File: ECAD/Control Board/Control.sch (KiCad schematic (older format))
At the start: 1 part

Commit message: control
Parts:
- added J?: FAN, symbol Connector:Conn_01x02_Female
- added Q? (x2): 2N7002, Package_TO_SOT_SMD:SOT-23, symbol Transistor_FET:2N7002
- added Q?: IRF7425, Package_SO:SOIC-8_3.9x4.9mm_P1.27mm, symbol Transistor_FET:IRF7404
- added R? (x2): 10K, symbol Device:R
- added R?: 100R, symbol Device:R
- added SW?: EN, symbol Switch:SW_SPST
- added SW?: Rotary_Encoder_Switch, symbol Device:Rotary_Encoder_Switch
- added U?: STM32BluePill, symbol symbols:STM32BluePill
- added U?: RC1602A, Display:RC1602A, symbol Display_Character:RC1602A
- added U?: 74HC595, symbol 74xx:74HC595
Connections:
- net +5V: now also Q?.5 (D), Q?.6 (D), Q?.7 (D), Q?.8 (D), R?.1, U?.18 (5V)
- net EN: now also Q?.3 (D), SW?.2 (B)
- net GND: now also Q?.2 (S), SW?.1 (A), U?.19 (GND), U?.39 (GND), U?.40 (GND)
- net IOUTBUF: now also U?.27 (PA2)
- net I_IN: now also U?.25 (PA0)
- net M_CS0: now also U?.13 (PB5)
- net M_CS1: now also U?.12 (PB4)
- net M_LDAC0: now also U?.11 (PB3)
- net M_LDAC1: now also U?.10 (PA15)
- net M_MOSI: now also U?.32 (PA7)
- net M_SCK: now also U?.30 (PA5)
- net VIN_BUF: now also U?.26 (PA1)
- net VOUTBUF: now also U?.28 (PA3)
- new net: Q?.1 (G), U?.5 (PA8)
- new net: J?.1 (Pin_1), Q?.1 (S), Q?.2 (S), Q?.3 (S)
- new net: Q?.3 (D), Q?.4 (G), R?.2
- new net: J?.2 (Pin_2), Q?.2 (S), R?.2
- new net: Q?.1 (G), R?.1, R?.2
- new net DISP0: U?.15 (QA), U?.7 (DB0)
- new net DISP1: U?.1 (QB), U?.8 (DB1)
- new net DISP2: U?.2 (QC), U?.9 (DB2)
- new net DISP3: U?.10 (DB3), U?.3 (QD)
- new net DISP4: U?.11 (DB4), U?.4 (QE)
- new net DISP5: U?.12 (DB5), U?.5 (QF)
- new net DISP6: U?.13 (DB6), U?.6 (QG)
- new net DISP7: U?.14 (DB7), U?.7 (QH)
- new net FAN: R?.1, U?.33 (PB0)

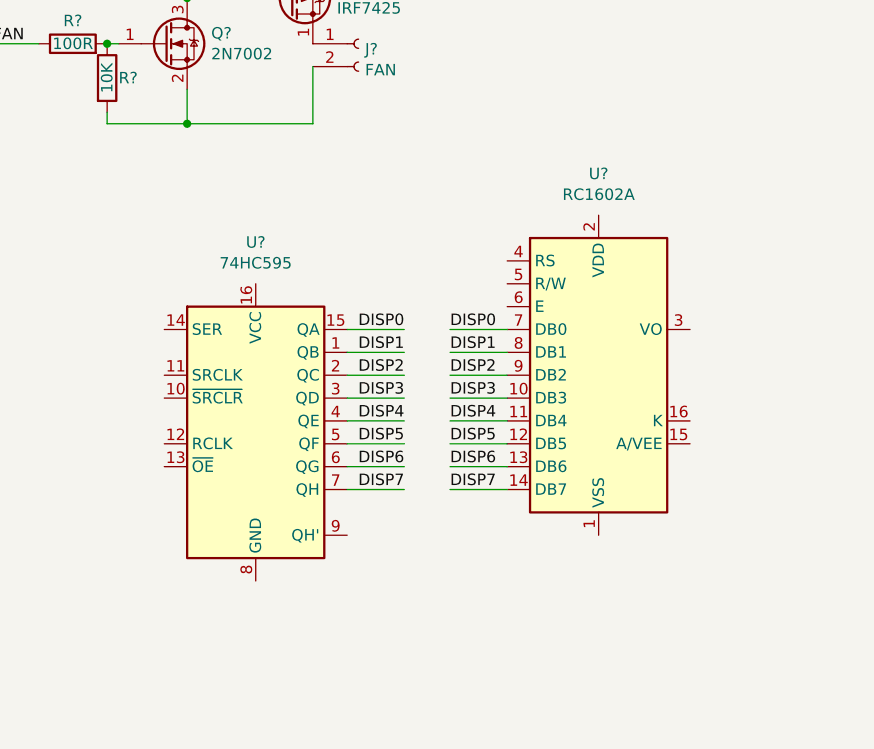
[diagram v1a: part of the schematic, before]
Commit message: connect parallel side of shift register
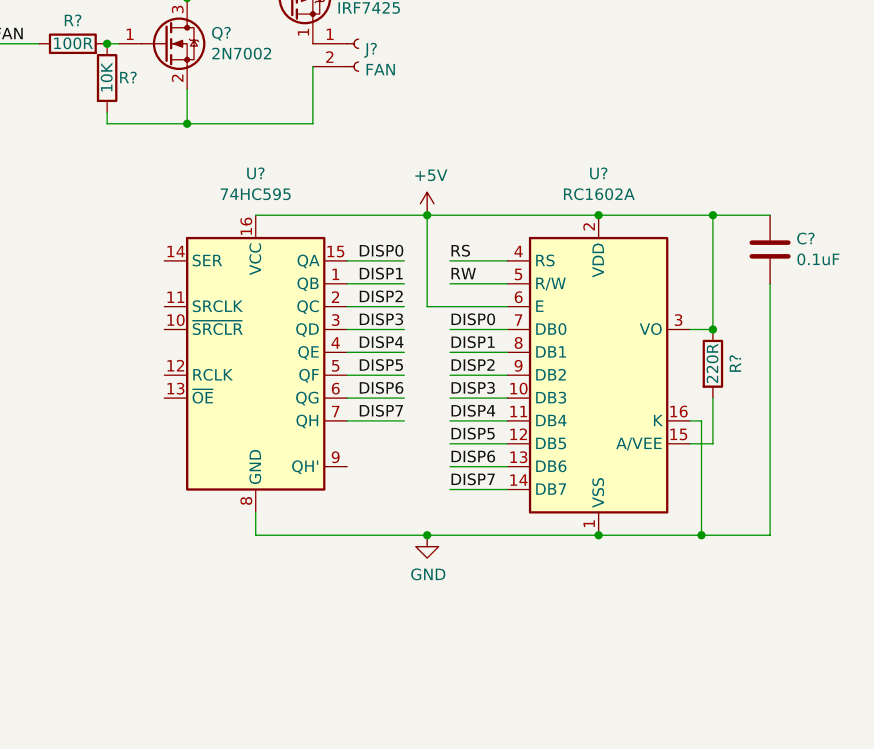
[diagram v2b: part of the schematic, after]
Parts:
- added C?: 0.1uF, symbol Device:C
- added R?: 220R, symbol Device:R
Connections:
- net +5V: now also U?.16 (VCC), U?.2 (VDD), U?.3 (VO), U?.6 (E), C?.1, R?.1
- net GND: now also U?.1 (VSS), U?.16 (K), U?.8 (GND), C?.2
- net at U?.15 (A/VEE): now also R?.2
- net RS: now reaches U?.4 (RS)
- net RW: now reaches U?.5 (R/W)
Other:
- moved on the sheet: U?
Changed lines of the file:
@@
 $EndComp
 Wire Wire Line
-	8500 3200 8250 3200
-Wire Wire Line
-	8500 3300 8250 3300
-Text Label 8500 3200 2    50   ~ 0
+	8500 2900 8250 2900
+Wire Wire Line
+	8500 3000 8250 3000
+Text Label 8500 2900 2    50   ~ 0
 DISP0
-Text Label 8500 3300 2    50   ~ 0
+Text Label 8500 3000 2    50   ~ 0
 DISP1
-Text Label 8500 3400 2    50   ~ 0
+Text Label 8500 3100 2    50   ~ 0
 DISP2
 Wire Wire Line
@@
 L 74xx:74HC595 U?
 U 1 1 62096F8C
-P 7850 3600
-F 0 "U?" H 7850 4381 50  0000 C CNN
-F 1 "74HC595" H 7850 4290 50  0000 C CNN
-F 2 "" H 7850 3600 50  0001 C CNN
-F 3 "http://www.ti.com/lit/ds/symlink/sn74hc595.pdf" H 7850 3600 50  0001 C CNN
-	1    7850 3600
-	1    0    0    -1
-$EndComp
-Text Label 8500 3900 2    50   ~ 0
+P 7850 3300
+F 0 "U?" H 7850 4081 50  0000 C CNN
+F 1 "74HC595" H 7850 3990 50  0000 C CNN
+F 2 "" H 7850 3300 50  0001 C CNN
+F 3 "http://www.ti.com/lit/ds/symlink/sn74hc595.pdf" H 7850 3300 50  0001 C CNN
+	1    7850 3300
+	1    0    0    -1
+$EndComp
+Text Label 8500 3600 2    50   ~ 0
 DISP7
-Text Label 8500 3800 2    50   ~ 0
+Text Label 8500 3500 2    50   ~ 0
 DISP6
-Text Label 8500 3700 2    50   ~ 0
+Text Label 8500 3400 2    50   ~ 0
 DISP5
-Text Label 8500 3600 2    50   ~ 0
+Text Label 8500 3300 2    50   ~ 0
 DISP4
 Wire Wire Line
-	8500 3900 8250 3900
-Wire Wire Line
-	8500 3800 8250 3800
-Wire Wire Line
-	8500 3700 8250 3700
-Wire Wire Line
 	8500 3600 8250 3600
 Wire Wire Line
-	8250 3400 8500 3400
-Text Label 8500 3500 2    50   ~ 0
+	8500 3500 8250 3500
+Wire Wire Line
+	8500 3400 8250 3400
+Wire Wire Line
+	8500 3300 8250 3300
+Wire Wire Line
+	8250 3100 8500 3100
+Text Label 8500 3200 2    50   ~ 0
 DISP3
 Wire Wire Line
-	8500 3500 8250 3500
+	8500 3200 8250 3200
 $Comp
 L Device:Rotary_Encoder_Switch SW?
@@
 	1    0    0    -1
 $EndComp
+Wire Wire Line
+	8700 3000 8950 3000
+Wire Wire Line
+	8950 2900 8700 2900
+Text Label 8700 3000 0    50   ~ 0
+RW
+Text Label 8700 2900 0    50   ~ 0
+RS
+Wire Wire Line
+	8600 3100 8600 2700
+Wire Wire Line
+	8600 2700 7850 2700
+Wire Wire Line
+	8600 3100 8950 3100
+Wire Wire Line
+	8600 2700 9350 2700
+Connection ~ 8600 2700
+Wire Wire Line
+	7850 4000 7850 4100
+Wire Wire Line
+	7850 4100 8600 4100
+Wire Wire Line
+	9750 3200 9850 3200
+Wire Wire Line
+	9850 3200 9850 2700
+Wire Wire Line
+	9850 2700 9350 2700
+Connection ~ 9350 2700
+Wire Wire Line
+	9750 3700 9850 3700
+$Comp
+L Device:R R?
+U 1 1 6208E94C
+P 9850 3350
+F 0 "R?" V 9950 3350 50  0000 C CNN
+F 1 "220R" V 9850 3350 50  0000 C CNN
+F 2 "" V 9780 3350 50  0001 C CNN
+F 3 "~" H 9850 3350 50  0001 C CNN
+	1    9850 3350
+	1    0    0    -1
+$EndComp
+Connection ~ 9850 3200
+Wire Wire Line
+	9850 3700 9850 3500
+Wire Wire Line
+	9750 3600 9800 3600
+Wire Wire Line
+	9800 3600 9800 4100
+Wire Wire Line
+	9800 4100 9350 4100
+Connection ~ 9350 4100
+$Comp
+L power:GND #PWR?
+U 1 1 62093C2C
+P 8600 4100
+F 0 "#PWR?" H 8600 3850 50  0001 C CNN
+F 1 "GND" H 8605 3927 50  0000 C CNN
+F 2 "" H 8600 4100 50  0001 C CNN
+F 3 "" H 8600 4100 50  0001 C CNN
+	1    8600 4100
+	1    0    0    -1
+$EndComp
+Connection ~ 8600 4100
+Wire Wire Line
+	8600 4100 9350 4100
+$Comp
+L power:+5V #PWR?
+U 1 1 6209452C
+P 8600 2700
+F 0 "#PWR?" H 8600 2550 50  0001 C CNN
+F 1 "+5V" H 8615 2873 50  0000 C CNN
+F 2 "" H 8600 2700 50  0001 C CNN
+F 3 "" H 8600 2700 50  0001 C CNN
+	1    8600 2700
+	1    0    0    -1
+$EndComp
+$Comp
+L Device:C C?
+U 1 1 62095008
+P 10100 2850
+F 0 "C?" H 10215 2896 50  0000 L CNN
+F 1 "0.1uF" H 10215 2805 50  0000 L CNN
+F 2 "" H 10138 2700 50  0001 C CNN
+F 3 "~" H 10100 2850 50  0001 C CNN
+	1    10100 2850
+	1    0    0    -1
+$EndComp
+Wire Wire Line
+	10100 2700 9850 2700
+Connection ~ 9850 2700
+Wire Wire Line
+	9800 4100 10100 4100
+Wire Wire Line
+	10100 4100 10100 3000
+Connection ~ 9800 4100
 $EndSCHEMATC

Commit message: Update Control.sch
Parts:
- added SW?: Rotary_Encoder_Switch, symbol Device:Rotary_Encoder_Switch
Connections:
- net +5V: now also U?.10 (~SRCLR)
- net GND: now also U?.13 (~OE)
- net LTCH2: now reaches U?.1 (PB12)
- net LTCH2: now also U?.12 (RCLK)
- net SCK2: now reaches U?.2 (PB13)
- net SCK2: now also U?.14 (SER)
- net MOSI2: now reaches U?.4 (PB15)
- net MOSI2: now also U?.11 (SRCLK)
- no-connect marks 0 -> 2
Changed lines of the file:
@@
 	10100 4100 10100 3000
 Connection ~ 9800 4100
+Text GLabel 5300 2600 0    50   Input ~ 0
+MOSI2
+Text GLabel 5300 2400 0    50   Input ~ 0
+SCK2
+Text GLabel 5300 2300 0    50   Input ~ 0
+LTCH2
+Text GLabel 7450 3100 0    50   Input ~ 0
+MOSI2
+Text GLabel 7450 2900 0    50   Input ~ 0
+SCK2
+Text GLabel 7450 3400 0    50   Input ~ 0
+LTCH2
+Wire Wire Line
+	7450 3500 7350 3500
+Wire Wire Line
+	7350 3500 7350 4100
+Wire Wire Line
+	7350 4100 7850 4100
+Connection ~ 7850 4100
+Wire Wire Line
+	7450 3200 7150 3200
+Wire Wire Line
+	7150 3200 7150 2700
+Wire Wire Line
+	7150 2700 7850 2700
+Connection ~ 7850 2700
+NoConn ~ 6300 3200
+NoConn ~ 5300 2500
+$Comp
+L Device:Rotary_Encoder_Switch SW?
+U 1 1 620AA3D9
+P 5550 5700
+F 0 "SW?" H 5550 6067 50  0000 C CNN
+F 1 "Rotary_Encoder_Switch" H 5550 5976 50  0000 C CNN
+F 2 "" H 5400 5860 50  0001 C CNN
+F 3 "~" H 5550 5960 50  0001 C CNN
+	1    5550 5700
+	1    0    0    -1
+$EndComp
 $EndSCHEMATC

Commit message: stuff
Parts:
- removed R?: 220R, symbol Device:R
- added RV?: 10K, symbol Device:R_POT_TRIM
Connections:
- net RW is gone; now on net GND: U?.5 (R/W)
- net +5V: now also U?.15 (A/VEE), RV?.3; no longer U?.3 (VO), U?.6 (E)
- net GND: now also RV?.1
- new net: RV?.2, U?.3 (VO)
- new net E: U?.6 (E)
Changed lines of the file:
@@
 $EndComp
 Wire Wire Line
-	8700 3000 8950 3000
+	8700 3100 8950 3100
 Wire Wire Line
 	8950 2900 8700 2900
-Text Label 8700 3000 0    50   ~ 0
-RW
+Text Label 8700 3100 0    50   ~ 0
+E
 Text Label 8700 2900 0    50   ~ 0
 RS
 Wire Wire Line
-	8600 3100 8600 2700
-Wire Wire Line
 	8600 2700 7850 2700
 Wire Wire Line
-	8600 3100 8950 3100
+	8600 3000 8950 3000
 Wire Wire Line
 	8600 2700 9350 2700
@@
 	7850 4100 8600 4100
 Wire Wire Line
-	9750 3200 9850 3200
-Wire Wire Line
-	9850 3200 9850 2700
-Wire Wire Line
 	9850 2700 9350 2700
 Connection ~ 9350 2700
 Wire Wire Line
 	9750 3700 9850 3700
-$Comp
-L Device:R R?
-U 1 1 6208E94C
-P 9850 3350
-F 0 "R?" V 9950 3350 50  0000 C CNN
-F 1 "220R" V 9850 3350 50  0000 C CNN
-F 2 "" V 9780 3350 50  0001 C CNN
-F 3 "~" H 9850 3350 50  0001 C CNN
-	1    9850 3350
-	1    0    0    -1
-$EndComp
-Connection ~ 9850 3200
-Wire Wire Line
-	9850 3700 9850 3500
 Wire Wire Line
 	9750 3600 9800 3600
@@
 	1    0    0    -1
 $EndComp
+Wire Wire Line
+	9850 2700 9850 3700
+$Comp
+L Device:R_POT_TRIM RV?
+U 1 1 620B7C18
+P 10450 3200
+F 0 "RV?" H 10380 3154 50  0000 R CNN
+F 1 "10K" V 10450 3200 50  0000 C CNN
+F 2 "" H 10450 3200 50  0001 C CNN
+F 3 "~" H 10450 3200 50  0001 C CNN
+	1    10450 3200
+	-1   0    0    1
+$EndComp
+Wire Wire Line
+	10450 3050 10450 2700
+Connection ~ 10100 2700
+Wire Wire Line
+	10100 4100 10450 4100
+Wire Wire Line
+	10450 4100 10450 3350
+Connection ~ 10100 4100
+Wire Wire Line
+	10450 2700 10100 2700
+Wire Wire Line
+	10300 3200 9750 3200
+Wire Wire Line
+	8600 4100 8600 3000
 $EndSCHEMATC

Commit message: add sw
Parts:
- added SW? (x2): SW_Push, symbol Switch:SW_Push
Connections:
- net E: now also U?.2 (QC)
- net RS: now also U?.1 (QB)
- net DISP0: no longer names the net of U?.7 (DB0)
- net DISP0: no longer U?.15 (QA)
- net DISP1: no longer names the net of U?.8 (DB1)
- net DISP1: no longer U?.1 (QB)
- net DISP2: no longer names the net of U?.9 (DB2)
- net DISP2: no longer U?.2 (QC)
- net DISP3: no longer names the net of U?.10 (DB3)
- net DISP3: no longer U?.3 (QD)
- no-connect marks 2 -> 6
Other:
- moved on the sheet: SW?
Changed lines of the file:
@@
 $EndComp
-Wire Wire Line
-	8500 2900 8250 2900
-Wire Wire Line
-	8500 3000 8250 3000
-Text Label 8500 2900 2    50   ~ 0
-DISP0
-Text Label 8500 3000 2    50   ~ 0
-DISP1
-Text Label 8500 3100 2    50   ~ 0
-DISP2
-Wire Wire Line
-	8700 3500 8950 3500
-Wire Wire Line
-	8950 3400 8700 3400
-Text Label 8700 3400 0    50   ~ 0
-DISP2
-Text Label 8700 3500 0    50   ~ 0
-DISP3
-Wire Wire Line
-	8950 3200 8700 3200
-Wire Wire Line
-	8950 3300 8700 3300
-Text Label 8700 3200 0    50   ~ 0
-DISP0
-Text Label 8700 3300 0    50   ~ 0
-DISP1
 Wire Wire Line
 	8950 3600 8700 3600
@@
 Wire Wire Line
 	8500 3300 8250 3300
-Wire Wire Line
-	8250 3100 8500 3100
-Text Label 8500 3200 2    50   ~ 0
-DISP3
-Wire Wire Line
-	8500 3200 8250 3200
 $Comp
 L Device:Rotary_Encoder_Switch SW?
 U 1 1 620A0B03
-P 5550 5000
-F 0 "SW?" H 5550 5367 50  0000 C CNN
-F 1 "Rotary_Encoder_Switch" H 5550 5276 50  0000 C CNN
-F 2 "" H 5400 5160 50  0001 C CNN
-F 3 "~" H 5550 5260 50  0001 C CNN
-	1    5550 5000
-	1    0    0    -1
-$EndComp
-Wire Wire Line
-	8700 3100 8950 3100
+P 3450 3150
+F 0 "SW?" H 3450 3517 50  0000 C CNN
+F 1 "Rotary_Encoder_Switch" H 3450 3426 50  0000 C CNN
+F 2 "" H 3300 3310 50  0001 C CNN
+F 3 "~" H 3450 3410 50  0001 C CNN
+	1    3450 3150
+	1    0    0    -1
+$EndComp
 Wire Wire Line
 	8950 2900 8700 2900
-Text Label 8700 3100 0    50   ~ 0
-E
 Text Label 8700 2900 0    50   ~ 0
 RS
@@
 L Device:Rotary_Encoder_Switch SW?
 U 1 1 620AA3D9
-P 5550 5700
-F 0 "SW?" H 5550 6067 50  0000 C CNN
-F 1 "Rotary_Encoder_Switch" H 5550 5976 50  0000 C CNN
-F 2 "" H 5400 5860 50  0001 C CNN
-F 3 "~" H 5550 5960 50  0001 C CNN
-	1    5550 5700
+P 3450 3850
+F 0 "SW?" H 3450 4217 50  0000 C CNN
+F 1 "Rotary_Encoder_Switch" H 3450 4126 50  0000 C CNN
+F 2 "" H 3300 4010 50  0001 C CNN
+F 3 "~" H 3450 4110 50  0001 C CNN
+	1    3450 3850
 	1    0    0    -1
 $EndComp
@@
 U 1 1 620B7C18
 P 10450 3200
-F 0 "RV?" H 10380 3154 50  0000 R CNN
+F 0 "RV?" H 10400 3200 50  0000 R CNN
 F 1 "10K" V 10450 3200 50  0000 C CNN
 F 2 "" H 10450 3200 50  0001 C CNN
@@
 Wire Wire Line
 	8600 4100 8600 3000
+Wire Wire Line
+	8250 3000 8500 3000
+Text Label 8500 3000 2    50   ~ 0
+RS
+Text Label 8700 3100 0    50   ~ 0
+E
+Wire Wire Line
+	8700 3100 8950 3100
+Text Label 8500 3100 2    50   ~ 0
+E
+Wire Wire Line
+	8500 3100 8250 3100
+NoConn ~ 8950 3200
+NoConn ~ 8950 3300
+NoConn ~ 8950 3400
+NoConn ~ 8950 3500
+$Comp
+L Switch:SW_Push SW?
+U 1 1 620D0CDE
+P 3450 2500
+F 0 "SW?" H 3450 2785 50  0000 C CNN
+F 1 "SW_Push" H 3450 2694 50  0000 C CNN
+F 2 "" H 3450 2700 50  0001 C CNN
+F 3 "~" H 3450 2700 50  0001 C CNN
+	1    3450 2500
+	1    0    0    -1
+$EndComp
+$Comp
+L Switch:SW_Push SW?
+U 1 1 620D1AF5
+P 3450 2050
+F 0 "SW?" H 3450 2335 50  0000 C CNN
+F 1 "SW_Push" H 3450 2244 50  0000 C CNN
+F 2 "" H 3450 2250 50  0001 C CNN
+F 3 "~" H 3450 2250 50  0001 C CNN
+	1    3450 2050
+	1    0    0    -1
+$EndComp
 $EndSCHEMATC

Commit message: Update Control.sch
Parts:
- removed SW?: Rotary_Encoder_Switch, symbol Device:Rotary_Encoder_Switch
- SW?: value SW_Push -> L
- SW?: value SW_Push -> R
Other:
- moved on the sheet: SW?
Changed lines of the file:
@@
 Wire Wire Line
 	8500 3300 8250 3300
-$Comp
-L Device:Rotary_Encoder_Switch SW?
-U 1 1 620A0B03
-P 3450 3150
-F 0 "SW?" H 3450 3517 50  0000 C CNN
-F 1 "Rotary_Encoder_Switch" H 3450 3426 50  0000 C CNN
-F 2 "" H 3300 3310 50  0001 C CNN
-F 3 "~" H 3450 3410 50  0001 C CNN
-	1    3450 3150
-	1    0    0    -1
-$EndComp
 Wire Wire Line
 	8950 2900 8700 2900
@@
 L Switch:SW_Push SW?
 U 1 1 620D0CDE
-P 3450 2500
-F 0 "SW?" H 3450 2785 50  0000 C CNN
-F 1 "SW_Push" H 3450 2694 50  0000 C CNN
-F 2 "" H 3450 2700 50  0001 C CNN
-F 3 "~" H 3450 2700 50  0001 C CNN
-	1    3450 2500
+P 3050 3450
+F 0 "SW?" H 3050 3735 50  0000 C CNN
+F 1 "L" H 3050 3644 50  0000 C CNN
+F 2 "" H 3050 3650 50  0001 C CNN
+F 3 "~" H 3050 3650 50  0001 C CNN
+	1    3050 3450
 	1    0    0    -1
 $EndComp
@@
 L Switch:SW_Push SW?
 U 1 1 620D1AF5
-P 3450 2050
-F 0 "SW?" H 3450 2335 50  0000 C CNN
-F 1 "SW_Push" H 3450 2244 50  0000 C CNN
-F 2 "" H 3450 2250 50  0001 C CNN
-F 3 "~" H 3450 2250 50  0001 C CNN
-	1    3450 2050
+P 3850 3450
+F 0 "SW?" H 3850 3735 50  0000 C CNN
+F 1 "R" H 3850 3644 50  0000 C CNN
+F 2 "" H 3850 3650 50  0001 C CNN
+F 3 "~" H 3850 3650 50  0001 C CNN
+	1    3850 3450
 	1    0    0    -1
 $EndComp

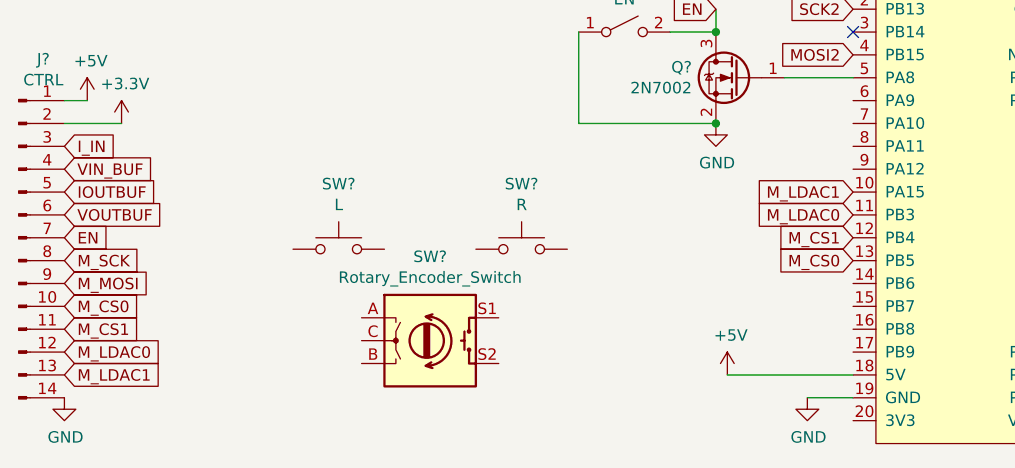
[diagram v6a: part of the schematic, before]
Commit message: Switch back to i2c control
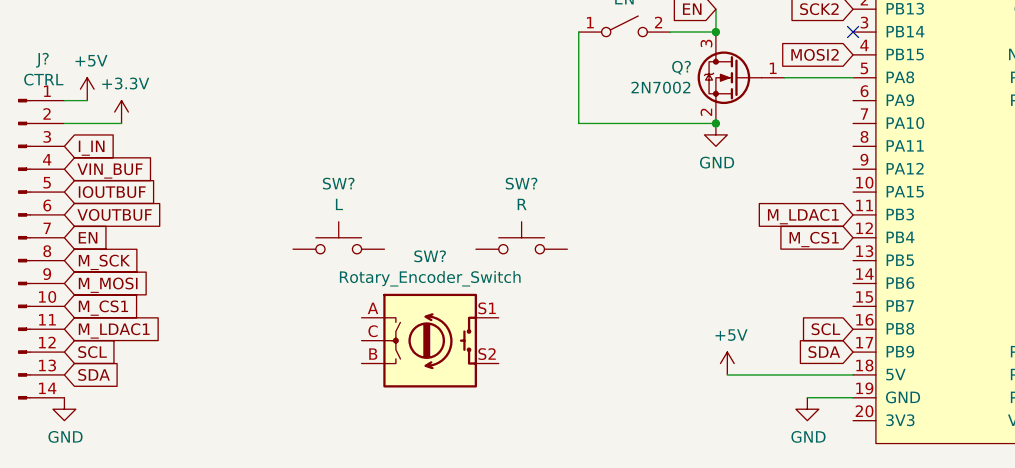
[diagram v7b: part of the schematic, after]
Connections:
- net M_CS1: now also J?.10 (Pin_10); no longer J?.11 (Pin_11)
- net M_LDAC1: now also J?.11 (Pin_11), U?.11 (PB3); no longer J?.13 (Pin_13), U?.10 (PA15)
- net SCL: now reaches U?.16 (PB8)
- net SCL: now also J?.12 (Pin_12)
- net SDA: now reaches U?.17 (PB9)
- net SDA: now also J?.13 (Pin_13)
- net M_CS0: no longer names the net of U?.13 (PB5)
- net M_CS0: no longer J?.10 (Pin_10)
- removed net M_LDAC0: J?.12 (Pin_12), U?.11 (PB3)
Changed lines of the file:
@@
 M_MOSI
 Text GLabel 1850 3700 2    50   Input ~ 0
-M_CS0
+M_CS1
 Text GLabel 1850 3800 2    50   Input ~ 0
-M_CS1
-Text GLabel 1850 3900 2    50   Input ~ 0
-M_LDAC0
-Text GLabel 1850 4000 2    50   Input ~ 0
 M_LDAC1
 $Comp
@@
 Text GLabel 6300 3500 2    50   Input ~ 0
 VOUTBUF
-Text GLabel 5300 3500 0    50   Input ~ 0
-M_CS0
 Text GLabel 5300 3400 0    50   Input ~ 0
 M_CS1
 Text GLabel 5300 3300 0    50   Input ~ 0
-M_LDAC0
-Text GLabel 5300 3200 0    50   Input ~ 0
 M_LDAC1
 $Comp
@@
 	1    0    0    -1
 $EndComp
+Text GLabel 1850 3900 2    50   Input ~ 0
+SCL
+Text GLabel 1850 4000 2    50   Input ~ 0
+SDA
+Text GLabel 5300 3800 0    50   Input ~ 0
+SCL
+Text GLabel 5300 3900 0    50   Input ~ 0
+SDA
 $EndSCHEMATC
